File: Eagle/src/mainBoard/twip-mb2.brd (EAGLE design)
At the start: 82.2 x 82.5 mm, 17 parts, among them U1 GY-521MPU6050

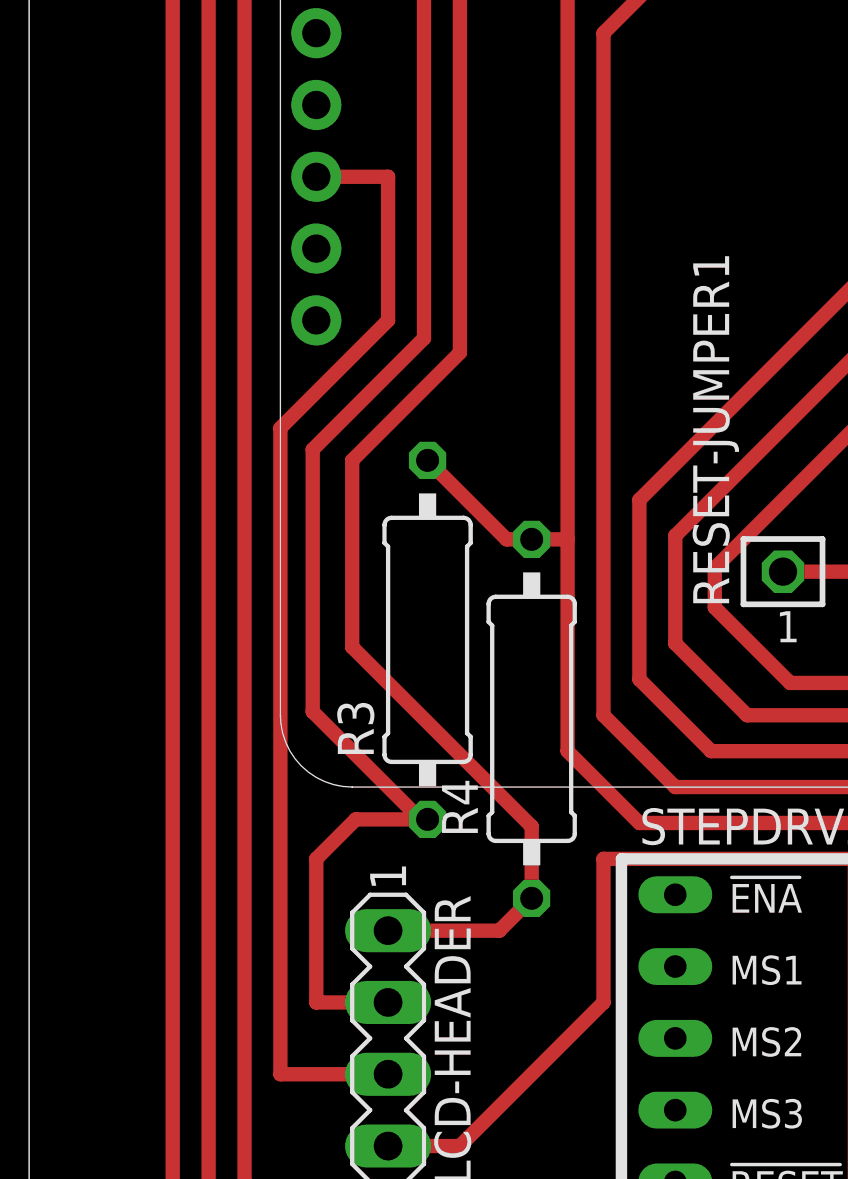
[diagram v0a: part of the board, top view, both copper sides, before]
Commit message: Update twip-mb2.brd
uncross I2C leads on LCD cable/header
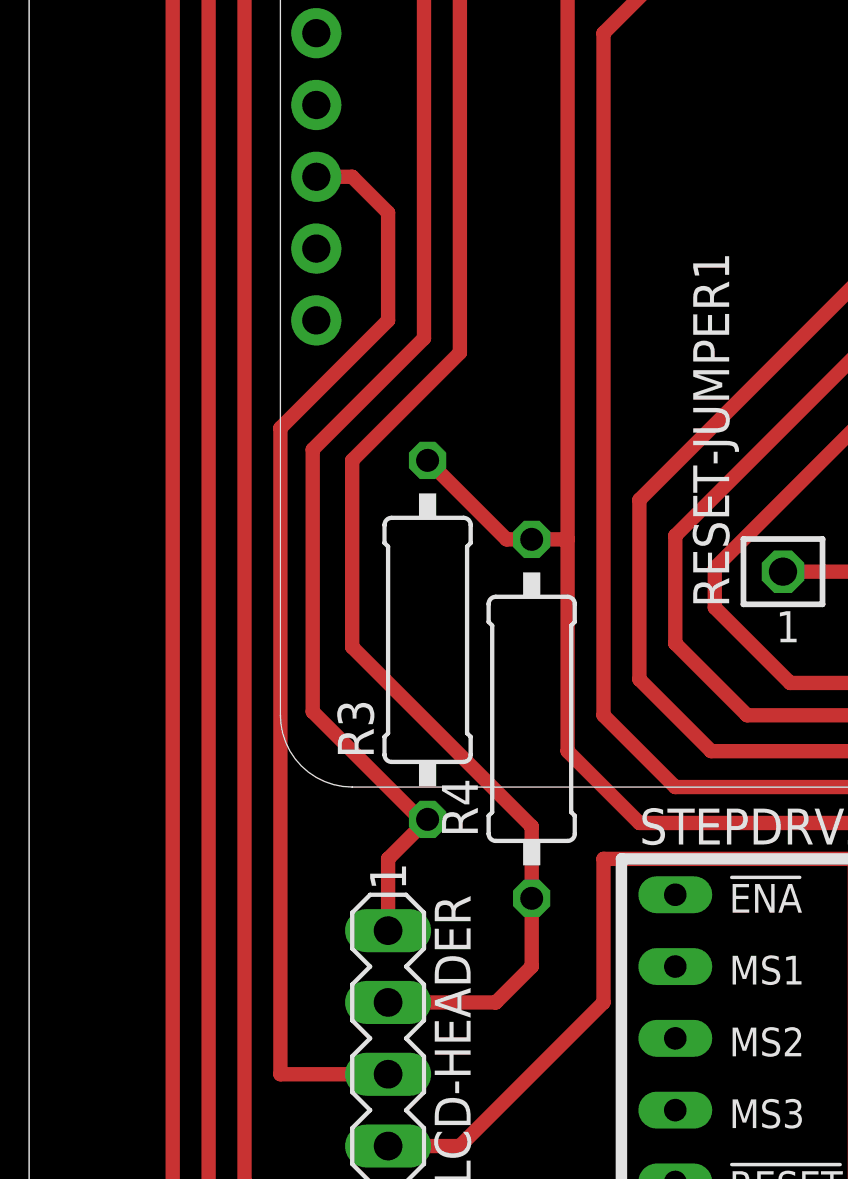
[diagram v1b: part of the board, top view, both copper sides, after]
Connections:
- net N$11: now also LCD-HEADER.1; no longer LCD-HEADER.2
- net N$19: now also LCD-HEADER.2; no longer LCD-HEADER.1
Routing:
- net N$11: track 63.7 -> 54.8 mm
- net N$19: track 63.2 -> 65.7 mm
- net USB: track 39.7 -> 38.9 mm
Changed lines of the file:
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@@
 <wire x1="15.24" y1="73.66" x2="15.24" y2="44.577" width="0.508" layer="1"/>
 <wire x1="10.16" y1="73.66" x2="15.24" y2="73.66" width="0.508" layer="1"/>
-<contactref element="LCD-HEADER" pad="1"/>
 <contactref element="R4" pad="1"/>
-<wire x1="17.78" y1="25.273" x2="16.637" y2="24.13" width="0.508" layer="1"/>
-<wire x1="12.7" y1="24.13" x2="16.637" y2="24.13" width="0.508" layer="1"/>
 <wire x1="17.78" y1="25.273" x2="17.78" y2="27.813" width="0.508" layer="1"/>
 <wire x1="17.78" y1="27.813" x2="11.43" y2="34.163" width="0.508" layer="1"/>
 <wire x1="11.43" y1="34.163" x2="11.43" y2="40.767" width="0.508" layer="1"/>
 <wire x1="11.43" y1="40.767" x2="15.24" y2="44.577" width="0.508" layer="1"/>
+<contactref element="LCD-HEADER" pad="2"/>
+<wire x1="12.7" y1="21.59" x2="16.51" y2="21.59" width="0.508" layer="1"/>
+<wire x1="16.51" y1="21.59" x2="17.78" y2="22.86" width="0.508" layer="1"/>
+<wire x1="17.78" y1="22.86" x2="17.78" y2="25.273" width="0.508" layer="1"/>
 </signal>
 <signal name="N$27">
@@
 <wire x1="8.89" y1="76.2" x2="8.89" y2="76.073" width="0" layer="19" extent="1-1"/>
 </signal>
-<signal name="N$11">
-<contactref element="LCD-HEADER" pad="2"/>
-<contactref element="MS2" pad="18"/>
-<wire x1="13.97" y1="21.59" x2="12.7" y2="21.59" width="0.508" layer="1"/>
-<wire x1="10.16" y1="71.12" x2="13.97" y2="71.12" width="0.508" layer="1"/>
-<wire x1="10.16" y1="21.59" x2="12.7" y2="21.59" width="0.508" layer="1"/>
-<wire x1="13.97" y1="71.12" x2="13.97" y2="45.085" width="0.508" layer="1"/>
-<contactref element="R3" pad="1"/>
-<wire x1="14.097" y1="28.067" x2="11.557" y2="28.067" width="0.508" layer="1"/>
-<wire x1="11.557" y1="28.067" x2="10.16" y2="26.67" width="0.508" layer="1"/>
-<wire x1="10.16" y1="26.67" x2="10.16" y2="21.59" width="0.508" layer="1"/>
-<wire x1="13.843" y1="28.067" x2="10.033" y2="31.877" width="0.508" layer="1"/>
-<wire x1="10.033" y1="31.877" x2="10.033" y2="41.148" width="0.508" layer="1"/>
-<wire x1="10.033" y1="41.148" x2="13.97" y2="45.085" width="0.508" layer="1"/>
-<wire x1="14.097" y1="28.067" x2="13.843" y2="28.067" width="0.508" layer="1"/>
-</signal>
 <signal name="N$21">
 <contactref element="IBC" pad="6"/>
@@
 <wire x1="8.89" y1="19.05" x2="8.89" y2="41.91" width="0.508" layer="1"/>
 <wire x1="8.89" y1="41.91" x2="12.7" y2="45.72" width="0.508" layer="1"/>
-<wire x1="12.7" y1="45.72" x2="12.7" y2="50.8" width="0.508" layer="1"/>
-<wire x1="12.7" y1="50.8" x2="10.16" y2="50.8" width="0.508" layer="1"/>
+<wire x1="12.7" y1="49.53" x2="12.7" y2="45.72" width="0.508" layer="1"/>
+<wire x1="10.16" y1="50.8" x2="11.43" y2="50.8" width="0.508" layer="1"/>
+<wire x1="11.43" y1="50.8" x2="12.7" y2="49.53" width="0.508" layer="1"/>
 </signal>
 <signal name="N$26">
@@
 <wire x1="67.31" y1="63.5" x2="72.39" y2="63.5" width="0.508" layer="1"/>
 </signal>
+<signal name="N$11">
+<contactref element="MS2" pad="18"/>
+<contactref element="R3" pad="1"/>
+<wire x1="10.16" y1="71.12" x2="13.97" y2="71.12" width="0.508" layer="1"/>
+<wire x1="13.97" y1="71.12" x2="13.97" y2="45.085" width="0.508" layer="1"/>
+<wire x1="13.843" y1="28.067" x2="10.033" y2="31.877" width="0.508" layer="1"/>
+<wire x1="10.033" y1="31.877" x2="10.033" y2="41.148" width="0.508" layer="1"/>
+<wire x1="10.033" y1="41.148" x2="13.97" y2="45.085" width="0.508" layer="1"/>
+<wire x1="14.097" y1="28.067" x2="13.843" y2="28.067" width="0.508" layer="1"/>
+<contactref element="LCD-HEADER" pad="1"/>
+<wire x1="12.7" y1="24.13" x2="12.7" y2="26.67" width="0.508" layer="1"/>
+<wire x1="12.7" y1="26.67" x2="14.097" y2="28.067" width="0.508" layer="1"/>
+</signal>
 </signals>

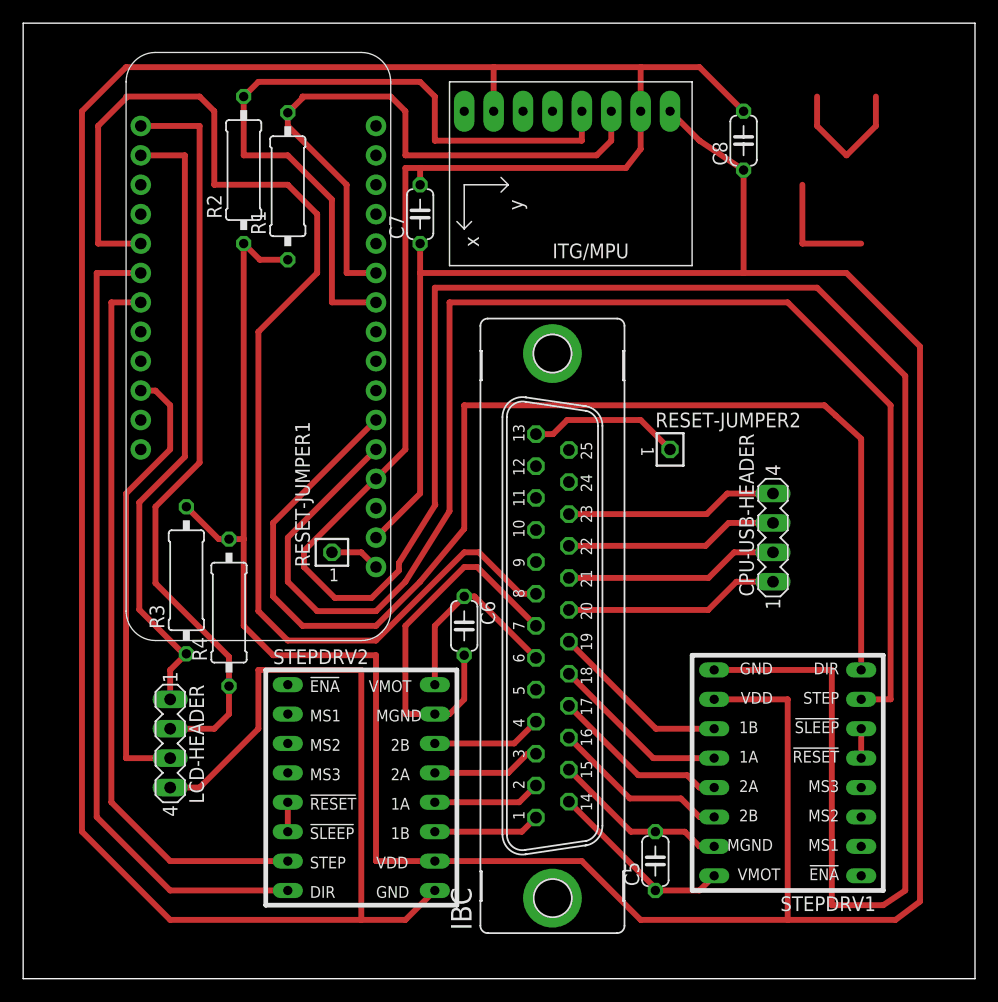
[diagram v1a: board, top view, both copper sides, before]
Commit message: Update twip-mb2.brd
major changes - requires PB2
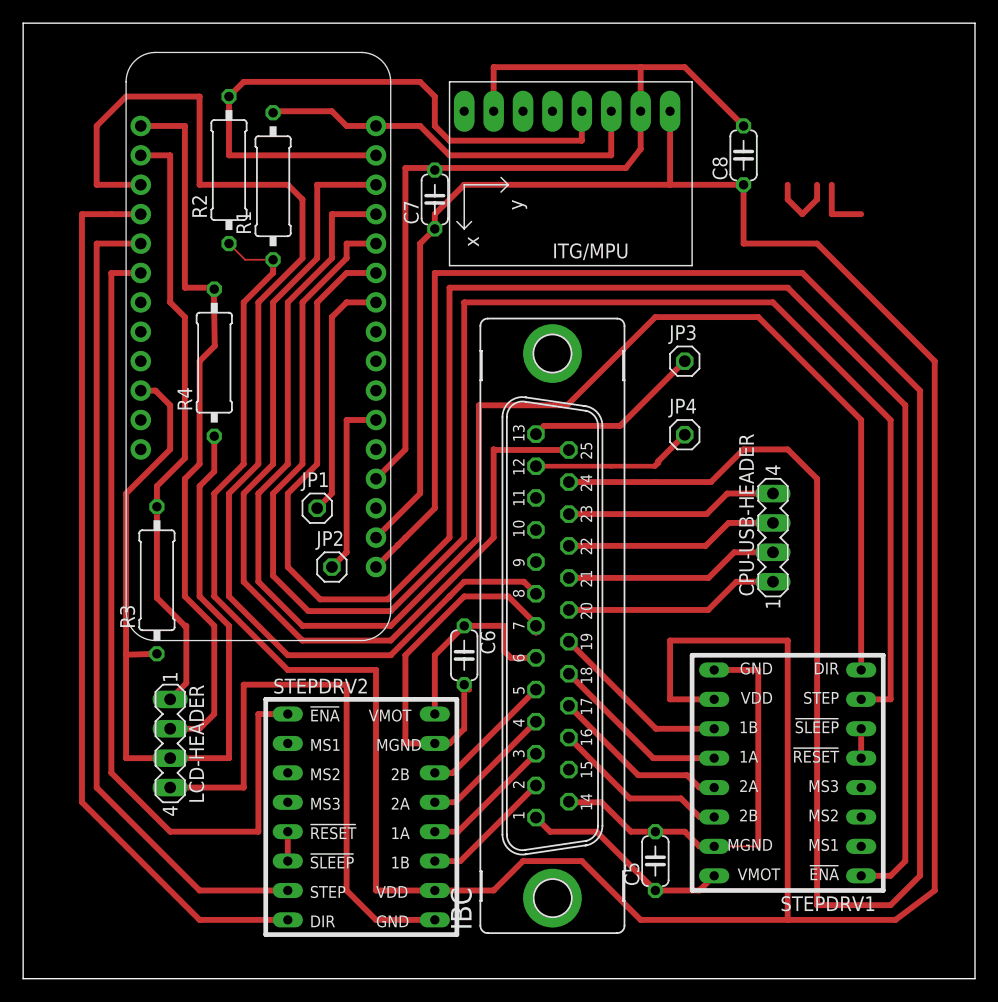
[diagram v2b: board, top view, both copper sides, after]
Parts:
- removed RESET-JUMPER1, RESET-JUMPER2: TSW-101-07-G-S, con-samtec:TSW-101-XX-G-S
- added JP1, JP2, JP3, JP4: (no value), pinhead:1X01
- R3, R4: value 2K2 -> 4K7
- moved R4 21.6 mm to (16.5, 53.2)
- moved STEPDRV2 2.54 mm to (30.5, 15.2)
- moved C6 2.54 mm to (38.1, 27.9)
- moved R3 2.54 mm to (11.6, 34.4)
- moved C7 1.80 mm to (35.6, 67.3)
- moved R1 1.27 mm to (21.6, 68.5)
- moved R2 1.27 mm to (17.8, 69.8)
- moved C8 1.27 mm to (62.2, 71.1)
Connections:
- removed net N$1: IBC.13, RESET-JUMPER2.1
- new net N$31: JP1.1, MS2.10
- new net N$32: MS2.11, STEPDRV1.1
- new net N$33: C6.2, IBC.7, LCD-HEADER.4, STEPDRV2.15, STEPDRV2.9
- new net N$34: MS2.22, STEPDRV2.1
- new net N$36: JP2.1, MS2.6
- new net N$37: IBC.13, JP3.1
- new net N$38: IBC.12, JP4.1
- net 3V: no longer R3.2, R4.2
- net N$10: now also IBC.4; no longer IBC.3
- net N$11: now also R3.2; no longer R3.1
- net N$12: now also IBC.5; no longer IBC.4
- net N$15: now also MS2.13; no longer MS2.6
- net N$16: now also IBC.24; no longer RESET-JUMPER1.1
- net N$17: now also MS2.16; no longer MS2.11
- net N$19: now also IBC.25, MS2.14; no longer LCD-HEADER.2, MS2.17, R4.1
- net N$2: now also C7.2, C8.2, MS2.4, U1.ADO, U1.GND; no longer C6.2, IBC.7, STEPDRV2.15
- net N$20: now also IBC.14, STEPDRV1.9; no longer IBC.15
- net N$22: now also IBC.1; no longer IBC.14
- net N$25: now also MS2.15; no longer MS2.10
- net N$27: now also MS2.20; no longer MS2.22
- net N$28: now also MS2.19; no longer MS2.21
- net N$29: now also MS2.21; no longer MS2.23
- net N$35: now also LCD-HEADER.2, MS2.17, R4.2; no longer C7.2, C8.2, LCD-HEADER.4, MS2.4, STEPDRV1.9, STEPDRV2.9, U1.ADO, U1.GND
- net N$5: now also MS2.12; no longer MS2.5
- net N$8: now also IBC.2; no longer IBC.1
- net N$9: now also IBC.3; no longer IBC.2
- net USB: now also R3.1, R4.1
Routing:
- net N$35: track 435.3 -> 63.5 mm
- net N$16: track 4.34 -> 186.0 mm
- net N$32: track 0.00 -> 156.3 mm
- net N$33: track 0.00 -> 83.8 mm
- net N$34: track 0.00 -> 73.2 mm
- net N$2: track 32.5 -> 83.8 mm
- net USB: track 38.9 -> 76.1 mm
- net N$15: track 106.3 -> 134.9 mm
- net N$20: track 15.3 -> 37.0 mm
- net N$5: track 121.8 -> 142.3 mm
- net N$19: track 65.7 -> 83.5 mm
- net N$17: track 54.5 -> 37.3 mm
- net 3V: track 286.6 -> 302.5 mm
- net N$36: track 0.00 -> 15.8 mm
- net N$37: track 0.00 -> 15.5 mm
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
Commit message: Update twip-mb2.brd
a few pin changes, all documented in pinouts doc.
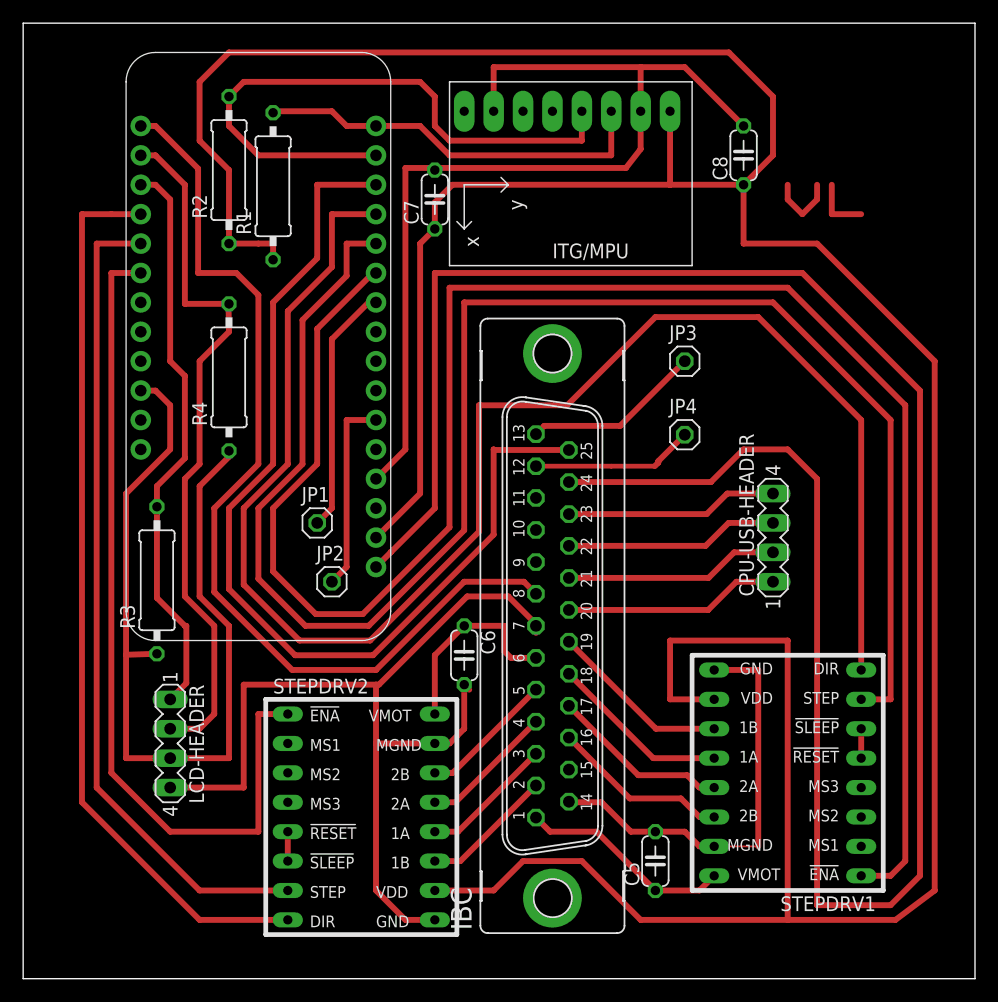
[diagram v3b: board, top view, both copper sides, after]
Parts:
- moved R4 1.80 mm to (17.8, 51.9)
- moved JP1 1.27 mm to (25.4, 39.4)
- moved JP2 1.27 mm to (26.7, 34.3)
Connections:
- net N$11: now also MS2.19; no longer MS2.18
- net N$28: now also MS2.17; no longer MS2.19
- net N$35: now also MS2.18; no longer MS2.17
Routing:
- net N$28: track 104.5 -> 82.9 mm
- net 3V: track 302.5 -> 307.8 mm
- net N$11: track 52.8 -> 49.5 mm
- net N$19: track 83.5 -> 86.6 mm
- net N$15: track 134.9 -> 137.6 mm
- net N$5: track 142.3 -> 144.9 mm
- net N$35: track 63.5 -> 61.4 mm
- net N$25: track 54.9 -> 53.4 mm
- net N$33: track 83.8 -> 82.4 mm
- net N$36: track 15.8 -> 17.0 mm
- net N$32: track 156.3 -> 157.5 mm
- net USB: track 76.1 -> 75.5 mm
